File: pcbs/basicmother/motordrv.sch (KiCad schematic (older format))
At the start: 22 parts

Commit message: Actualizo esquematico de la placa principal y empiezo con el layout
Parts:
- removed CBST_A?, CBST_B?, CBST_C?, CBST_D?, CPVDD_A?, CPVDD_B?, CPVDD_C?, CPVDD_D?, C_VREG?: 100 nF, symbol C
- removed CGVDD_A?, CGVDD_B?, CGVDD_C?, CGVDD_D?, CVDD?: 1 uF, symbol C
- removed CPVDD?: 10 nF, symbol C
- removed CPVDD?: 1000 uF, symbol CAPAPOL
- removed CVDD?: 330 uF, symbol CAPAPOL
- removed CVDD?: 47 uF, symbol CAPAPOL
- removed R?: 1, symbol R
- removed RPVDD?: 3.3, symbol R
- removed R_OC_ADJ?: 68 K, symbol R
- removed U?: DRV8432, MODULE, symbol DRV8432
- added C18, C20: 100n, Capacitors_ThroughHole:C_Disc_D3_P2.5, symbol C
- added C19: 10n, Capacitors_ThroughHole:C_Disc_D3_P2.5, symbol C
- added CVDD1: 330 uF, Capacitors_ThroughHole:C_Radial_D5_L6_P2.5, symbol CAPAPOL
- added IC2: DRV8843, Popurri_CDR:HTSSOP28, symbol DRV8843
- added R11, R12, R13: 10k, Resistors_ThroughHole:Resistor_Horizontal_RM10mm, symbol R
- added R14, R15: .47, Resistors_ThroughHole:Resistor_Horizontal_RM15mm, symbol R
- added R16: 1M, Resistors_ThroughHole:Resistor_Horizontal_RM10mm, symbol R
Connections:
- net labels added: INT33, IN_A1, IN_A2, IN_B1, IN_B2, MOUT_A1, MOUT_A2, MOUT_B1, MOUT_B2, OUT_A1, OUT_A2, OUT_B1, OUT_B2, ~RESET, ~SLEEP
- net labels removed: AGND, M1, M2, M3, MOUT_A, MOUT_B, MOUT_C, MOUT_D, OUT_A, OUT_B, OUT_C, OUT_D, PWM_A, PWM_B, PWM_C, PWM_D, ~OTW, ~RESET_AB, ~RESET_CD
- wire segments 42 -> 80
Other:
- note removed: "Mode selection pins: \nFull bridge mode"

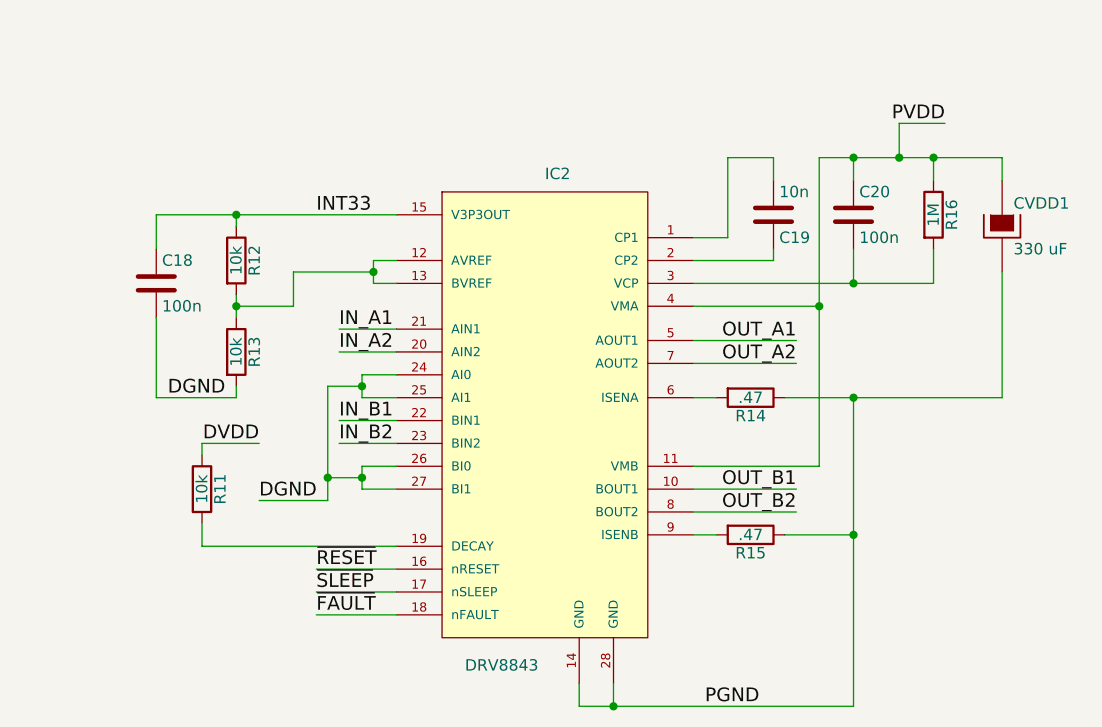
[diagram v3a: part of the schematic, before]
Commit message: saque el micro para el control de los ojitos y lo pase a una placa aparte, ademas agregue un doble microfono
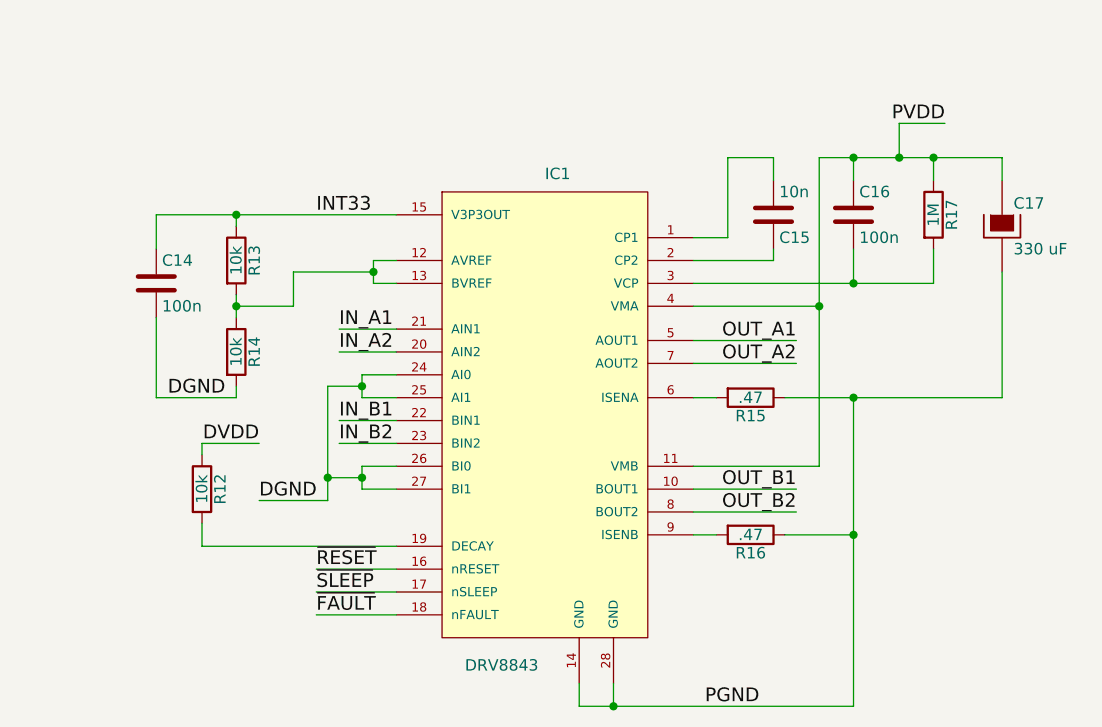
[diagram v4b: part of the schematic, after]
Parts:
- renumbered C18 to C14, C19 to C15, C20 to C16, CVDD1 to C17, IC2 to IC1, R11 to R12, R12 to R13, R13 to R14, R14 to R15, R15 to R16, R16 to R17
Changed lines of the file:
@@
 DVDD
 $Comp
-L DRV8843 IC2
+L DRV8843 IC1
 U 1 1 551F476F
 P 6300 3750
-F 0 "IC2" H 6300 4700 50  0000 L BNN
+F 0 "IC1" H 6300 4700 50  0000 L BNN
 F 1 "DRV8843" H 5950 2550 50  0000 L BNN
 F 2 "Popurri_CDR:HTSSOP28" H 7200 4850 50  0001 C CNN
@@
 $EndComp
 $Comp
-L C C19
+L C C15
 U 1 1 551F9CEB
 P 7300 2950
-F 0 "C19" H 7325 3050 50  0000 L CNN
+F 0 "C15" H 7325 3050 50  0000 L CNN
 F 1 "10n" H 7325 2850 50  0000 L CNN
 F 2 "Capacitors_ThroughHole:C_Disc_D3_P2.5" H 7338 2800 30  0001 C CNN
@@
 	7300 3150 6950 3150
 $Comp
-L C C20
+L C C16
 U 1 1 551F9F21
 P 7650 2950
-F 0 "C20" H 7675 3050 50  0000 L CNN
+F 0 "C16" H 7675 3050 50  0000 L CNN
 F 1 "100n" H 7675 2850 50  0000 L CNN
 F 2 "Capacitors_ThroughHole:C_Disc_D3_P2.5" H 7688 2800 30  0001 C CNN
@@
 	7650 3250 7650 3100
 $Comp
-L R R16
+L R R17
 U 1 1 551FA163
 P 8000 2950
-F 0 "R16" V 8080 2950 50  0000 C CNN
+F 0 "R17" V 8080 2950 50  0000 C CNN
 F 1 "1M" V 8000 2950 50  0000 C CNN
 F 2 "Resistors_ThroughHole:Resistor_Horizontal_RM10mm" V 7930 2950 30  0001 C CNN
@@
 	7400 4150 6950 4150
 $Comp
-L R R14
+L R R15
 U 1 1 551FAE19
 P 7200 3750
-F 0 "R14" V 7280 3750 50  0000 C CNN
+F 0 "R15" V 7280 3750 50  0000 C CNN
 F 1 ".47" V 7200 3750 50  0000 C CNN
 F 2 "Resistors_ThroughHole:Resistor_Horizontal_RM15mm" V 7130 3750 30  0001 C CNN
@@
 	7650 3750 7650 5100
 $Comp
-L R R15
+L R R16
 U 1 1 551FAFC7
 P 7200 4350
-F 0 "R15" V 7280 4350 50  0000 C CNN
+F 0 "R16" V 7280 4350 50  0000 C CNN
 F 1 ".47" V 7200 4350 50  0000 C CNN
 F 2 "Resistors_ThroughHole:Resistor_Horizontal_RM15mm" V 7130 4350 30  0001 C CNN
@@
 IN_B2
 $Comp
-L C C18
+L C C14
 U 1 1 551FD325
 P 4600 3250
-F 0 "C18" H 4625 3350 50  0000 L CNN
+F 0 "C14" H 4625 3350 50  0000 L CNN
 F 1 "100n" H 4625 3150 50  0000 L CNN
 F 2 "Capacitors_ThroughHole:C_Disc_D3_P2.5" H 4638 3100 30  0001 C CNN
@@
 	4600 3400 4600 3750
 $Comp
-L R R12
+L R R13
 U 1 1 551FD567
 P 4950 3150
-F 0 "R12" V 5030 3150 50  0000 C CNN
+F 0 "R13" V 5030 3150 50  0000 C CNN
 F 1 "10k" V 4950 3150 50  0000 C CNN
 F 2 "Resistors_ThroughHole:Resistor_Horizontal_RM10mm" V 4880 3150 30  0001 C CNN
@@
 $EndComp
 $Comp
-L R R13
+L R R14
 U 1 1 551FD6E3
 P 4950 3550
-F 0 "R13" V 5030 3550 50  0000 C CNN
+F 0 "R14" V 5030 3550 50  0000 C CNN
 F 1 "10k" V 4950 3550 50  0000 C CNN
 F 2 "Resistors_ThroughHole:Resistor_Horizontal_RM10mm" V 4880 3550 30  0001 C CNN
@@
 PGND
 $Comp
-L CAPAPOL CVDD1
+L CAPAPOL C17
 U 1 1 551FF258
 P 8300 3000
-F 0 "CVDD1" H 8350 3100 50  0000 L CNN
+F 0 "C17" H 8350 3100 50  0000 L CNN
 F 1 "330 uF" H 8350 2900 50  0000 L CNN
 F 2 "Capacitors_ThroughHole:C_Radial_D5_L6_P2.5" H 8300 3000 60  0001 C CNN
@@
 	5350 4200 5050 4200
 $Comp
-L R R11
+L R R12
 U 1 1 551FF94C
 P 4800 4150
-F 0 "R11" V 4880 4150 50  0000 C CNN
+F 0 "R12" V 4880 4150 50  0000 C CNN
 F 1 "10k" V 4800 4150 50  0000 C CNN
 F 2 "Resistors_ThroughHole:Resistor_Horizontal_RM10mm" V 4730 4150 30  0001 C CNN
